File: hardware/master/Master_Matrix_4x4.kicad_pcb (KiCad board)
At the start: 2 copper layers, 192 x 192 mm, 79 parts, among them SW1 SW_SPDT, U1 esp32-wemos-d1-mini, U2 74AHCT1G125

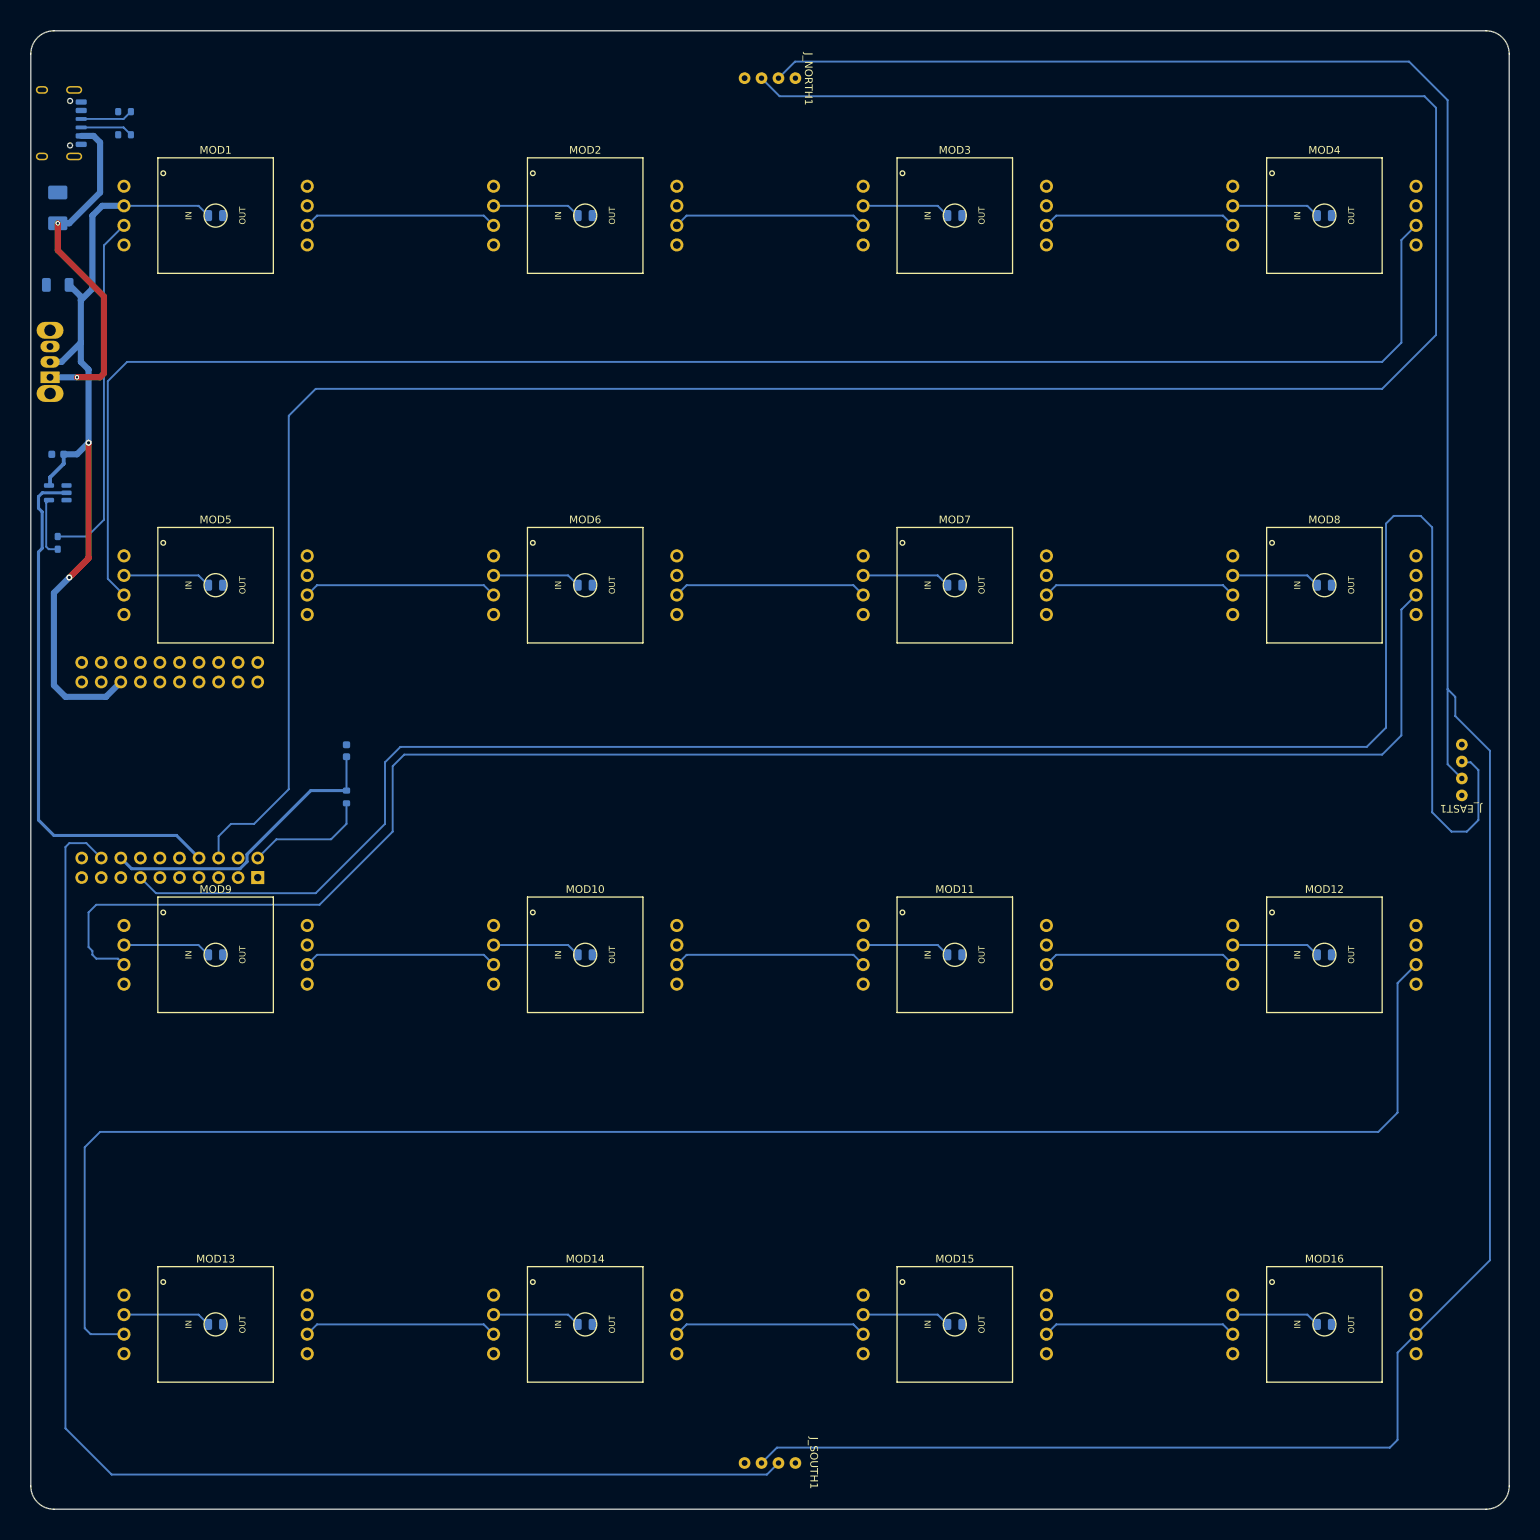
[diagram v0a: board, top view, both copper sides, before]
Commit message: feat(hardware): update Master PCB layout and Master/Slave 4x4 matrix schematics
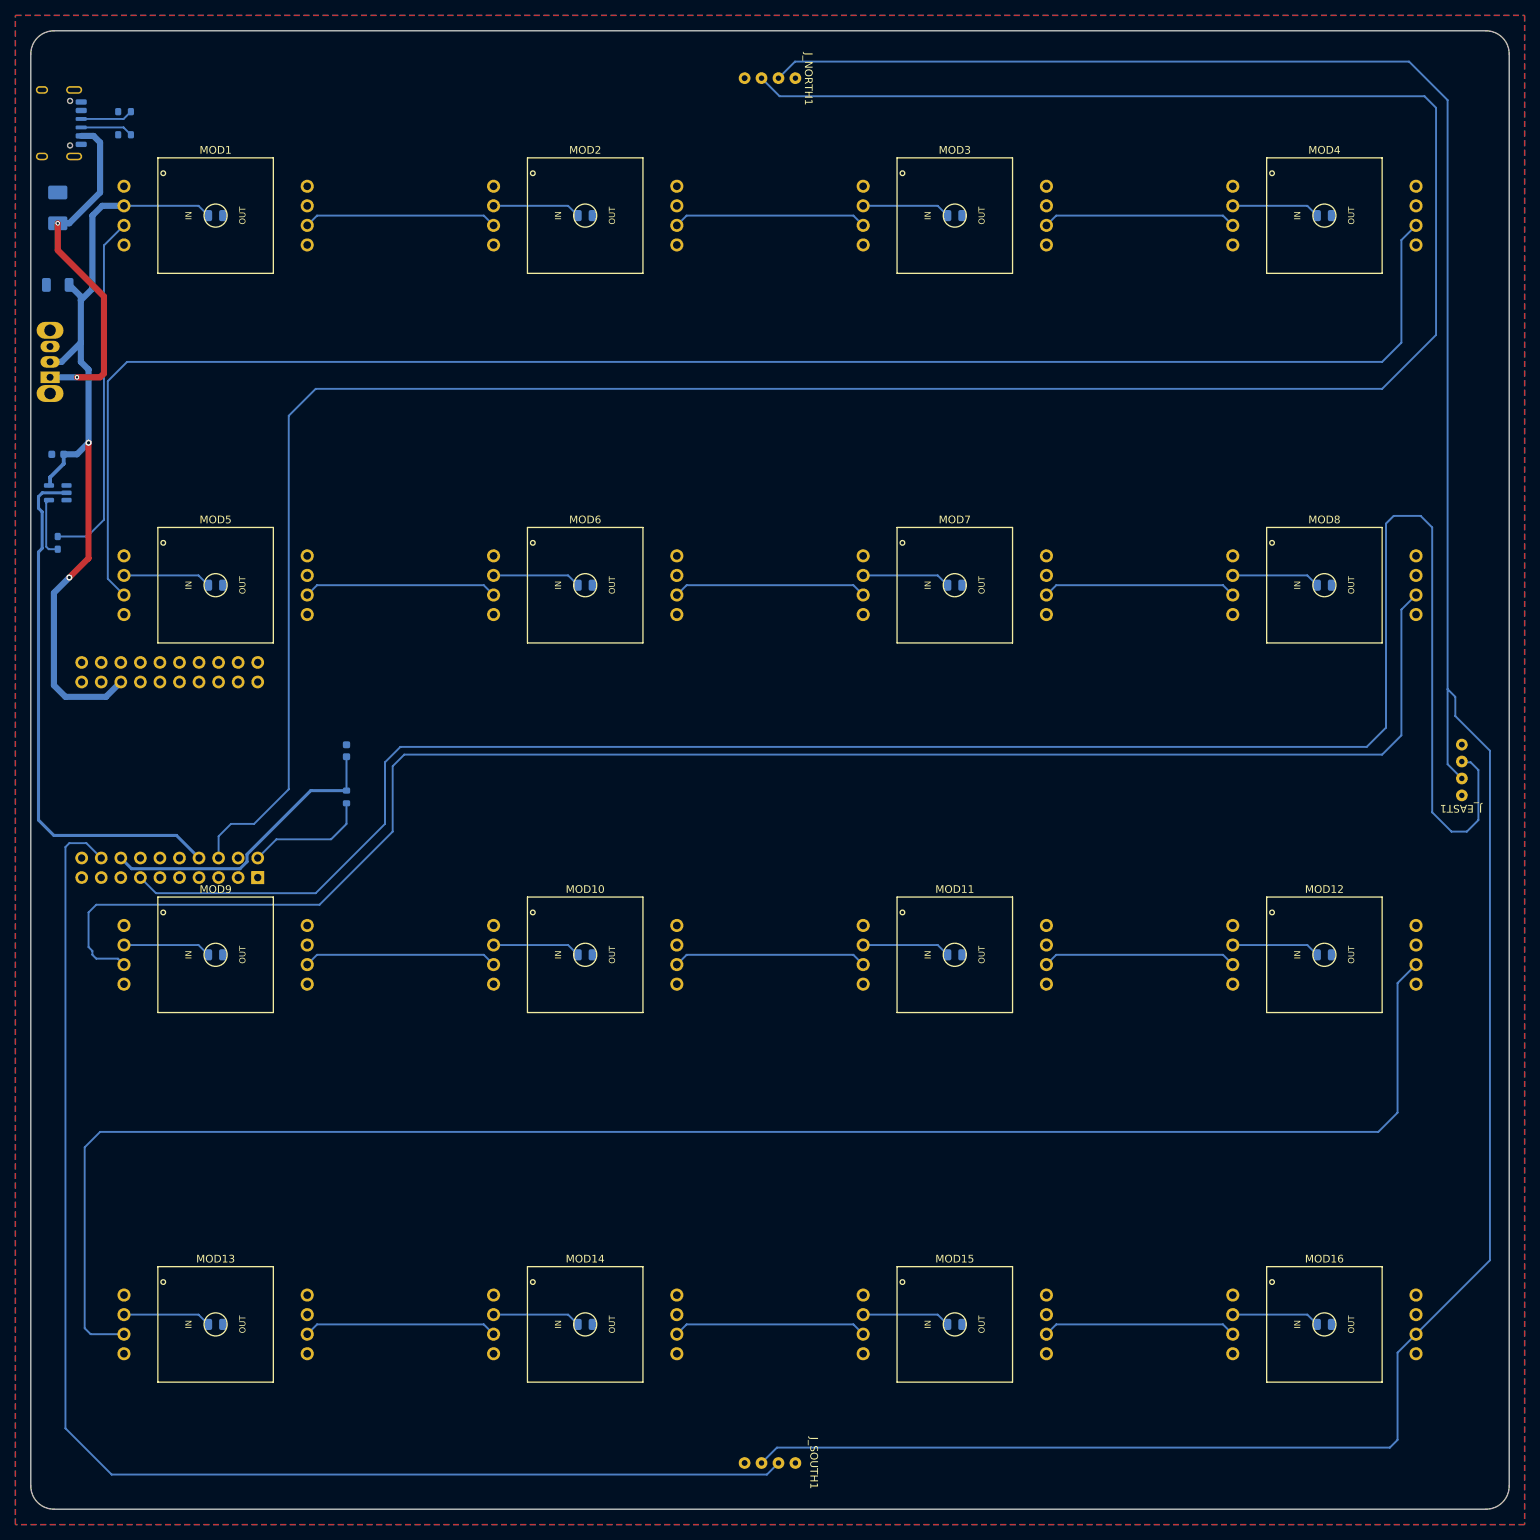
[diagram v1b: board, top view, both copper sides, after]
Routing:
- added copper zone on F.Cu, net +5V
- added copper zone on B.Cu, net GND
